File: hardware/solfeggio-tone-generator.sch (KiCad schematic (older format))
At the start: 13 parts

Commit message: Update schematic
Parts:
- removed R? (x4): 20k, symbol R
- removed R? (x3): 10k, symbol R
- added C? (x2): CP, symbol CP
- added C?: 100 nF, symbol C
- added D?: LED, symbol LED
- added DS?: EW162G5YMY, EW162G5YMY, symbol EW162G5YMY
- added J?: CONN_01X02, symbol CONN_01X02
- added R? (x24): 10k, symbol R
- added R?: 10 k, symbol R_Variable
- added R?: 18 k, symbol R
- added SW? (x2): SW_Push, symbol SW_Push
- added U?: 7805_oturpe, symbol 7805_oturpe
- R? (x2): value 20k -> 10k
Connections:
- net +5V: now also U?.20 (AVCC), U?.7 (VCC), C?.1, C?.1, DS?.17 (LED+), DS?.2 (VDD), R?.1, U?.3 (VO)
- net GND: now also U?.22 (GND), U?.8 (GND), C?.2, C?.2, C?.2, D?.1 (K), DS?.1 (VSS), DS?.18 (LED-), DS?.5 (R/~W), J?.1 (P1), R?.1, R?.2, SW?.2, SW?.2, U?.2 (GND)
- net 7: now reaches U?.10 ((PCINT7/XTAL2/TOSC2)PB7)
- net 7: now also DS?.14 (DB7)
- net at U?.11 ((PCINT21/OC0B/T1)PD5): now also R?.2, R?.2
- net at U?.12 ((PCINT22/OC0A/AIN0)PD6): now also R?.2, R?.2
- net at U?.13 ((PCINT23/AIN1)PD7): now also R?.2, R?.2
- net 0: now reaches U?.14 ((PCINT0/CLKO/ICP1)PB0)
- net 0: now also DS?.7 (DB0)
- net 1: now reaches U?.15 ((PCINT1/OC1A)PB1)
- net 1: now also DS?.8 (DB1)
- net 2: now reaches U?.16 ((PCINT2/OC1B/~SS~)PB2)
- net 2: now also DS?.9 (DB2)
- net at P?.4 (MOSI): no longer U?.17 ((PCINT3/OC2A/MOSI)PB3)
- net 4: now reaches P?.1 (MISO), U?.18 ((PCINT4/MISO)PB4)
- net 4: now also DS?.11 (DB4)
- net 5: now reaches P?.3 (SCK), U?.19 ((PCINT5/SCK)PB5)
- net 5: now also DS?.12 (DB5)
- net at R?.2, U?.2 ((PCINT16/RXD)PD0): now also R?.2
- net RS: now reaches U?.23 ((PCINT8/ADC0)PC0)
- net RS: now also DS?.4 (RS)
- net E: now reaches U?.24 ((PCINT9/ADC1)PC1)
- net E: now also DS?.6 (E)
- net at U?.26 ((PCINT11/ADC3)PC3): now also SW?.1
- net at U?.27 ((PCINT12/SDA/ADC4)PC4): now also SW?.1
- net at U?.28 ((PCINT13/SCL/ADC5)PC5): now also R?.2
- net at U?.3 ((PCINT17/TXD)PD1): now also R?.2, R?.2
- net at U?.4 ((PCINT18/INT0)PD2): now also R?.2, R?.2
- net at U?.5 ((PCINT19/OC2B/INT1)PD3): now also R?.2, R?.2
- net at U?.6 ((PCINT20/XCK/T0)PD4): now also R?.2, R?.2
- net 6: now reaches U?.9 ((PCINT6/XTAL1/TOSC1)PB6)
- net 6: now also DS?.13 (DB6)
- net at R?.1, R?.1, R?.2: now also R?.1, R?.2
- net at R?.2: now also R?.1, R?.1, R?.1
- net at J?.1 (P1): now also R?.2
- new net: R?.1, R?.1, R?.1, R?.2 (x6)
- new net: D?.2 (A), R?.1
- new net: C?.1, J?.2 (P2), U?.1 (VI)
- new net: DS?.3 (Vo), R?.1, R?.2
- new net 3: DS?.10 (DB3), U?.17 ((PCINT3/OC2A/MOSI)PB3)
- no-connect marks 0 -> 1
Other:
- moved on the sheet: J?, P?, R?

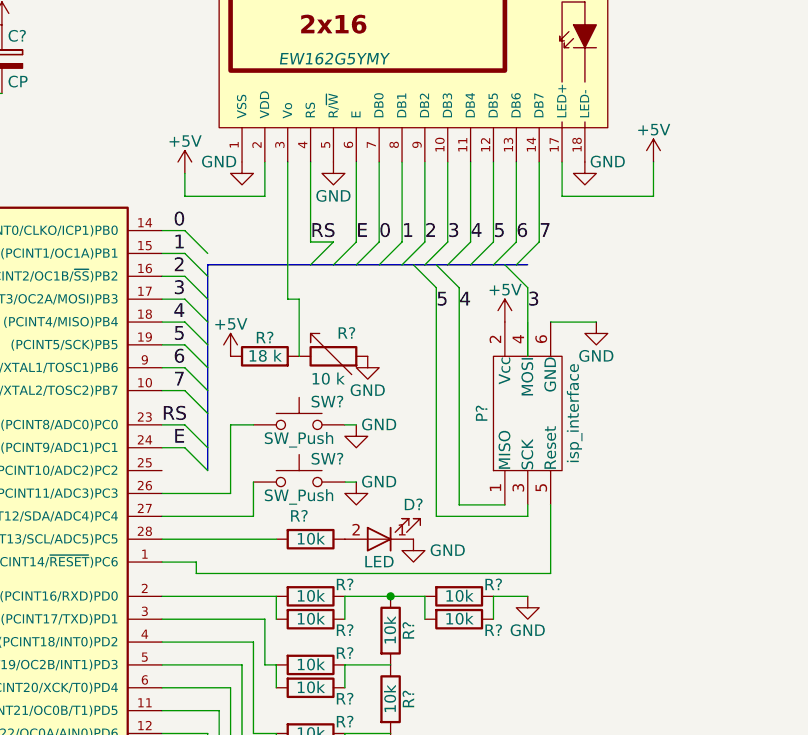
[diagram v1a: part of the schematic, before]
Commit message: Add crystal oscillator
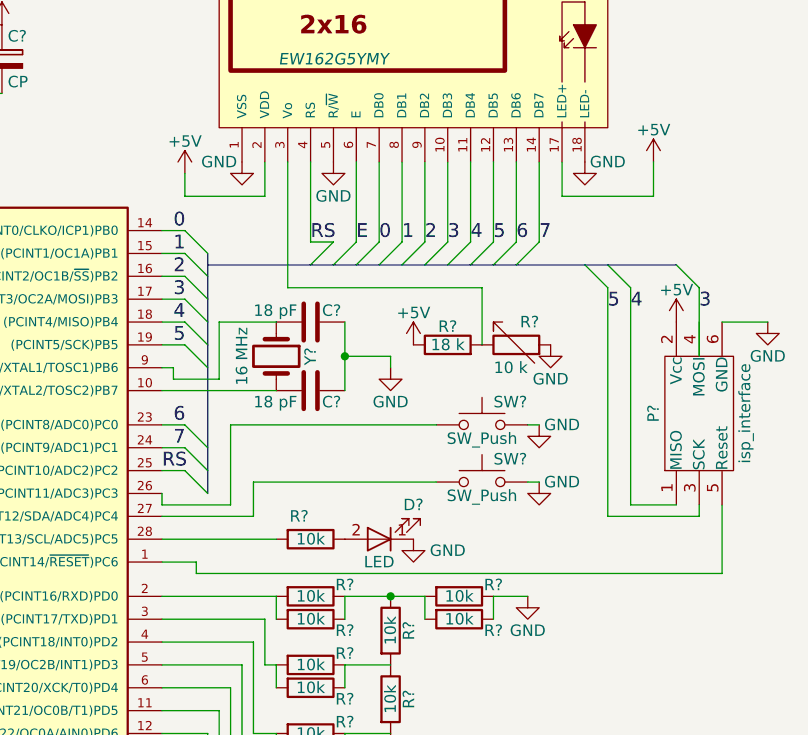
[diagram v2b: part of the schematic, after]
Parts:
- added C? (x2): 18 pF, symbol C
- added Y?: 16 MHz, symbol Crystal
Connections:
- net 6: now also U?.23 ((PCINT8/ADC0)PC0); no longer U?.9 ((PCINT6/XTAL1/TOSC1)PB6)
- net 7: now also U?.24 ((PCINT9/ADC1)PC1); no longer U?.10 ((PCINT7/XTAL2/TOSC2)PB7)
- net E: no longer U?.24 ((PCINT9/ADC1)PC1)
- net GND: now also C?.1, C?.1
- net RS: now also U?.25 ((PCINT10/ADC2)PC2); no longer U?.23 ((PCINT8/ADC0)PC0)
- new net: C?.2, U?.10 ((PCINT7/XTAL2/TOSC2)PB7), Y?.2
- new net: C?.2, U?.9 ((PCINT6/XTAL1/TOSC1)PB6), Y?.1
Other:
- moved on the sheet: P?, R?, SW?

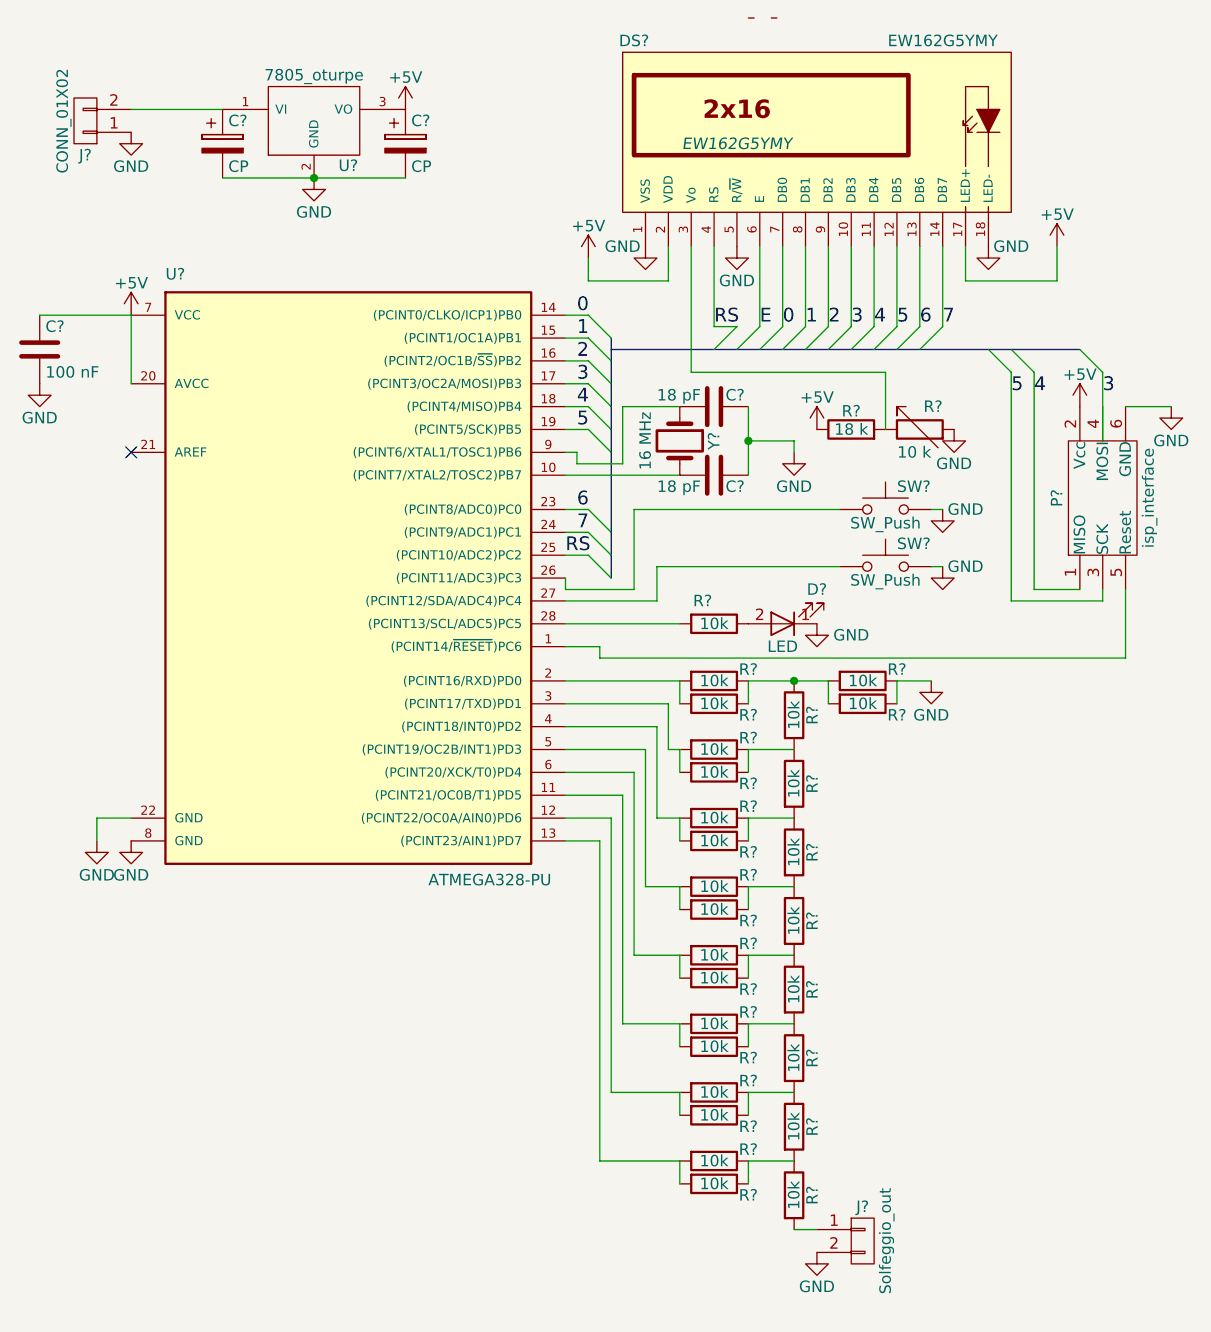
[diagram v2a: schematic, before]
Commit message: Add power polarity protection diode
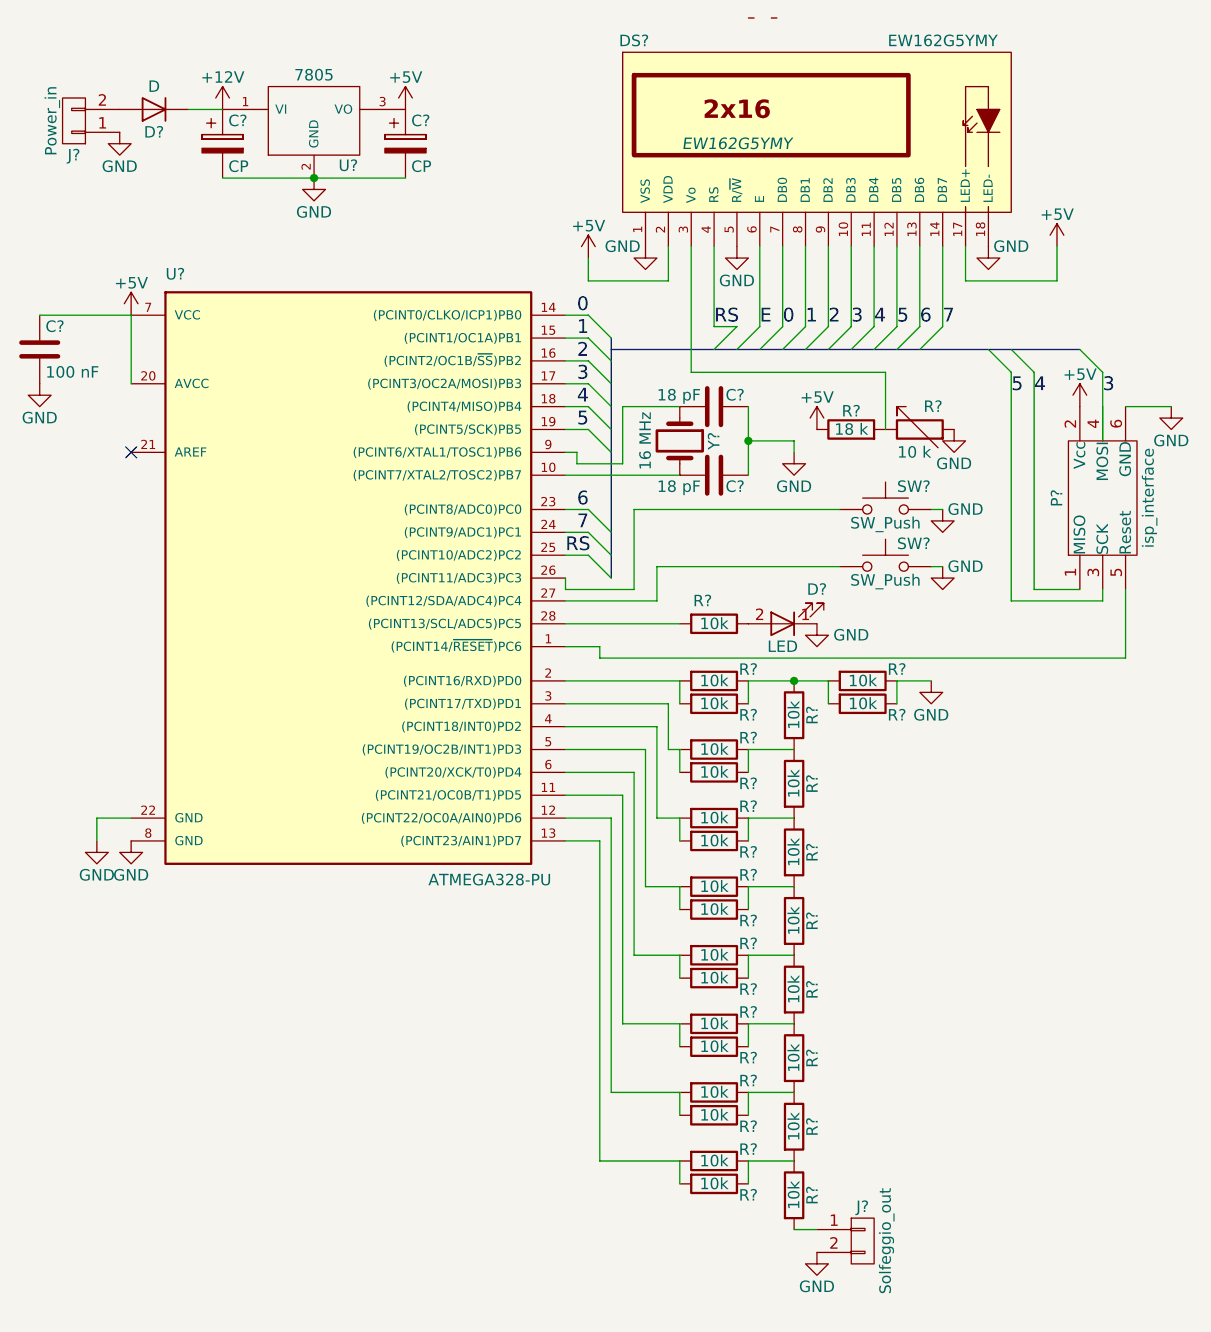
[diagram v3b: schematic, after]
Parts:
- added D?: D, symbol D
- J?: value CONN_01X02 -> Power_in
- U?: value 7805_oturpe -> 7805
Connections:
- net +12V: now reaches C?.1, U?.1 (VI)
- net +12V: now also D?.1 (K); no longer J?.2 (P2)
- new net: D?.2 (A), J?.2 (P2)
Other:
- moved on the sheet: J?
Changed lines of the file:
@@
 P 5400 1050
 F 0 "U?" H 5550 854 50  0000 C CNN
-F 1 "7805_oturpe" H 5400 1250 50  0000 C CNN
+F 1 "7805" H 5400 1250 50  0000 C CNN
 F 2 "" H 5400 1050 50  0000 C CNN
 F 3 "" H 5400 1050 50  0000 C CNN
@@
 L CONN_01X02 J?
 U 1 1 5AB9B263
-P 4400 1050
-F 0 "J?" H 4400 1200 50  0000 C CNN
-F 1 "CONN_01X02" V 4500 1050 50  0000 C CNN
-F 2 "" H 4400 1050 50  0001 C CNN
-F 3 "" H 4400 1050 50  0001 C CNN
-	1    4400 1050
+P 4350 1050
+F 0 "J?" H 4350 1200 50  0000 C CNN
+F 1 "Power_in" V 4450 1050 50  0000 C CNN
+F 2 "" H 4350 1050 50  0001 C CNN
+F 3 "" H 4350 1050 50  0001 C CNN
+	1    4350 1050
 	-1   0    0    1
 $EndComp
@@
 L GND #PWR?
 U 1 1 5AB9B2E8
-P 4600 1100
-F 0 "#PWR?" H 4600 850 50  0001 C CNN
-F 1 "GND" H 4600 950 50  0000 C CNN
-F 2 "" H 4600 1100 50  0001 C CNN
-F 3 "" H 4600 1100 50  0001 C CNN
-	1    4600 1100
+P 4550 1100
+F 0 "#PWR?" H 4550 850 50  0001 C CNN
+F 1 "GND" H 4550 950 50  0000 C CNN
+F 2 "" H 4550 1100 50  0001 C CNN
+F 3 "" H 4550 1100 50  0001 C CNN
+	1    4550 1100
 	1    0    0    -1
 $EndComp
@@
 	6500 3500 7000 3500
 Wire Wire Line
-	7300 3500 7500 3500
-Wire Wire Line
-	7500 3500 7650 3500
+	7300 3500 7650 3500
 Wire Wire Line
 	7950 3500 7950 3600
@@
 	7300 5600 7500 5600
 Wire Wire Line
-	5000 1300 5400 1300
-Wire Wire Line
-	5400 1300 5800 1300
+	5000 1300 5800 1300
 Connection ~ 5400 1300
-Wire Wire Line
-	4600 1000 5000 1000
 Wire Wire Line
 	4600 4100 4450 4100
@@
 	6600 1750 6600 1650
 Wire Bus Line
-	6700 2050 7150 2050
+	6700 2050 8750 2050
 Wire Bus Line
-	7150 2050 7250 2050
-Wire Bus Line
-	7250 2050 7350 2050
-Wire Bus Line
-	7350 2050 7450 2050
-Wire Bus Line
-	7450 2050 7550 2050
-Wire Bus Line
-	7550 2050 7650 2050
-Wire Bus Line
-	7650 2050 7750 2050
-Wire Bus Line
-	7750 2050 7850 2050
-Wire Bus Line
-	7850 2050 7950 2050
-Wire Bus Line
-	7950 2050 8050 2050
-Wire Bus Line
-	8050 2050 8350 2050
-Wire Bus Line
-	8350 2050 8450 2050
-Wire Bus Line
-	8450 2050 8750 2050
-Wire Bus Line
-	6700 2000 6700 2100
-Wire Bus Line
-	6700 2100 6700 2200
-Wire Bus Line
-	6700 2200 6700 2300
-Wire Bus Line
-	6700 2300 6700 2400
-Wire Bus Line
-	6700 2400 6700 2500
-Wire Bus Line
-	6700 2500 6700 2850
-Wire Bus Line
-	6700 2850 6700 2950
-Wire Bus Line
-	6700 2950 6700 3050
+	6700 2000 6700 3050
 Wire Wire Line
 	8250 1600 8250 1750
@@
 Wire Wire Line
 	6500 2950 6600 2950
-Wire Wire Line
-	6600 2950 6600 2950
 Wire Wire Line
 	6900 3000 6900 3150
@@
 $EndComp
 Wire Wire Line
-	7300 2300 7300 2450
-Wire Wire Line
-	7300 2450 7300 2600
+	7300 2300 7300 2600
 Wire Wire Line
 	7300 2450 7500 2450
@@
 Wire Wire Line
 	6500 3100 6800 3100
+$Comp
+L D D?
+U 1 1 5AC8C127
+P 4700 1000
+F 0 "D?" H 4700 1100 50  0000 C CNN
+F 1 "D" H 4700 900 50  0000 C CNN
+F 2 "" H 4700 1000 50  0001 C CNN
+F 3 "" H 4700 1000 50  0001 C CNN
+	1    4700 1000
+	-1   0    0    1
+$EndComp
+Wire Wire Line
+	4850 1000 5000 1000
+$Comp
+L +12V #PWR?
+U 1 1 5AC8C424
+P 5000 1000
+F 0 "#PWR?" H 5000 850 50  0001 C CNN
+F 1 "+12V" H 5000 1140 50  0000 C CNN
+F 2 "" H 5000 1000 50  0001 C CNN
+F 3 "" H 5000 1000 50  0001 C CNN
+	1    5000 1000
+	1    0    0    -1
+$EndComp
 $EndSCHEMATC
